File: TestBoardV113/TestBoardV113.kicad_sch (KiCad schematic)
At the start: 75 parts, among them J1 Conn_01x02_Socket, J10 Conn_01x02_Pin, J11 Conn_01x02_Pin, J12 Conn_02x03_Odd_Even, J13 Conn_01x01_Pin, J14 Conn_01x28_Socket, J15 Conn_01x01_Pin, J16 Conn_01x01_Pin, J17 Conn_01x02_Pin, J18 Conn_01x02_Socket, J19 Conn_01x28_Socket, J2 Conn_02x06_Odd_Even, J20 Conn_01x01_Pin, J21 Conn_01x02_Pin, J22 Conn_02x03_Odd_Even, J23 Conn_01x02_Pin, J24 Conn_01x02_Socket, J3 Conn_01x02_Pin, J4 Conn_01x02_Pin, J5 Conn_01x02_Pin, J6 Conn_01x02_Pin, J7 Conn_01x02_Pin, J8 Conn_01x02_Pin, J9 Conn_01x02_Pin, SW1 SW_DIP_x04, U3 NCP705MTADJTCG, U4 TAR5SxxU_SOT353F, U5 TXB0104PW, U6 TXB0104PW

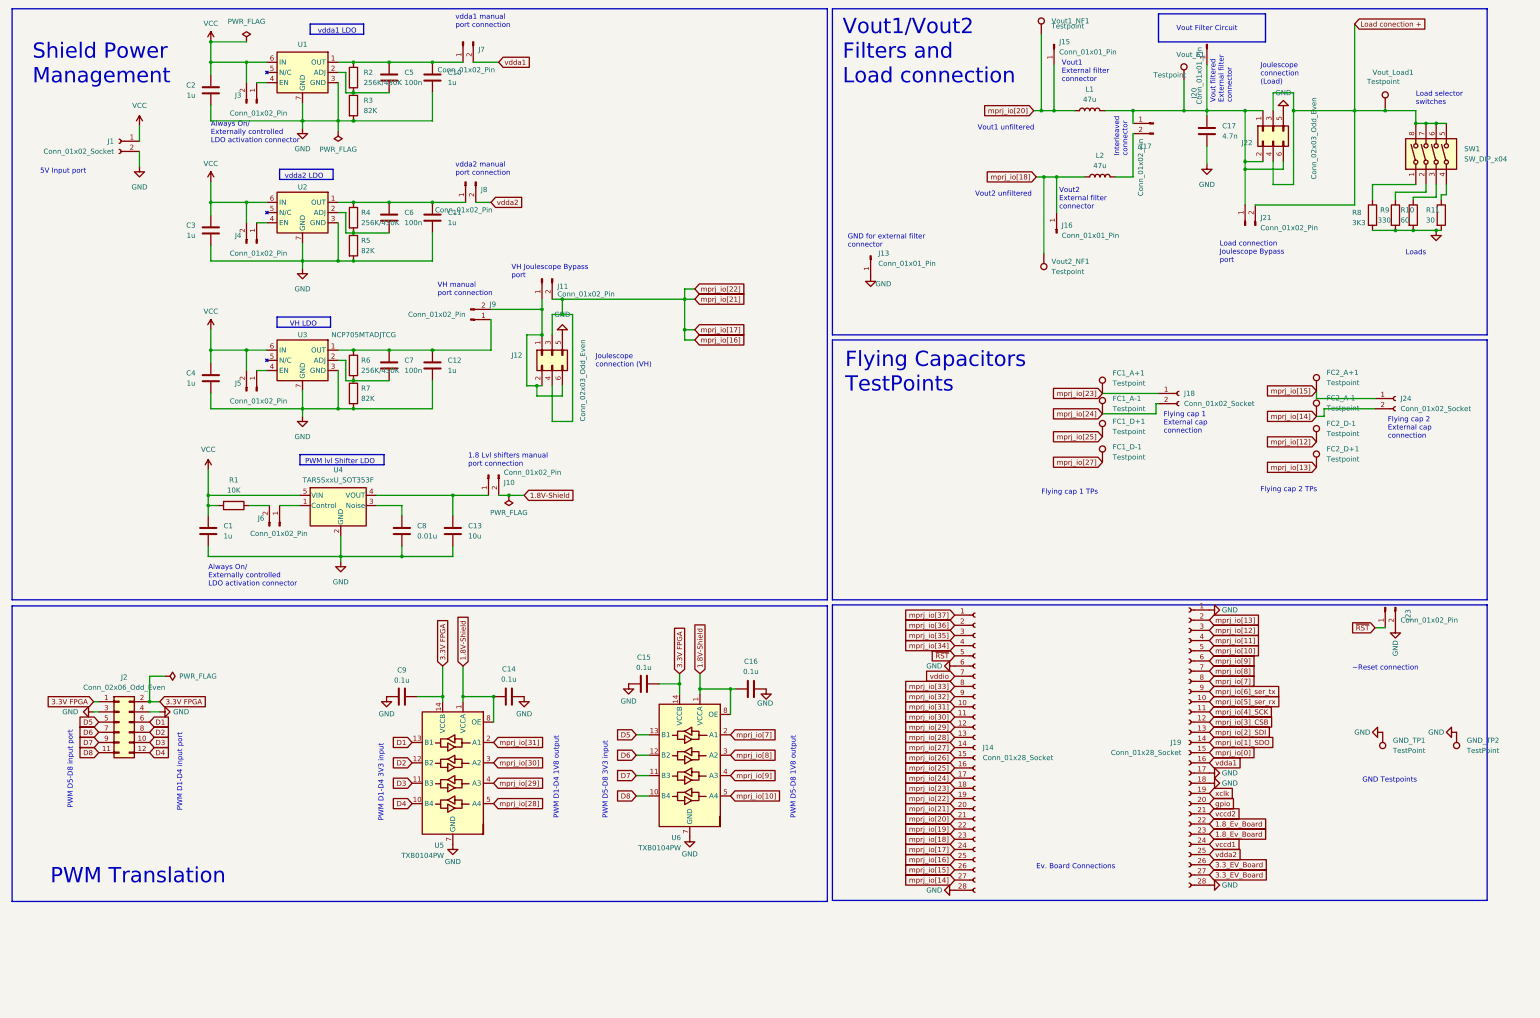
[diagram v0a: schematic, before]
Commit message: Added features
Added Joulescope port for efficiency measurement with and without level shifters
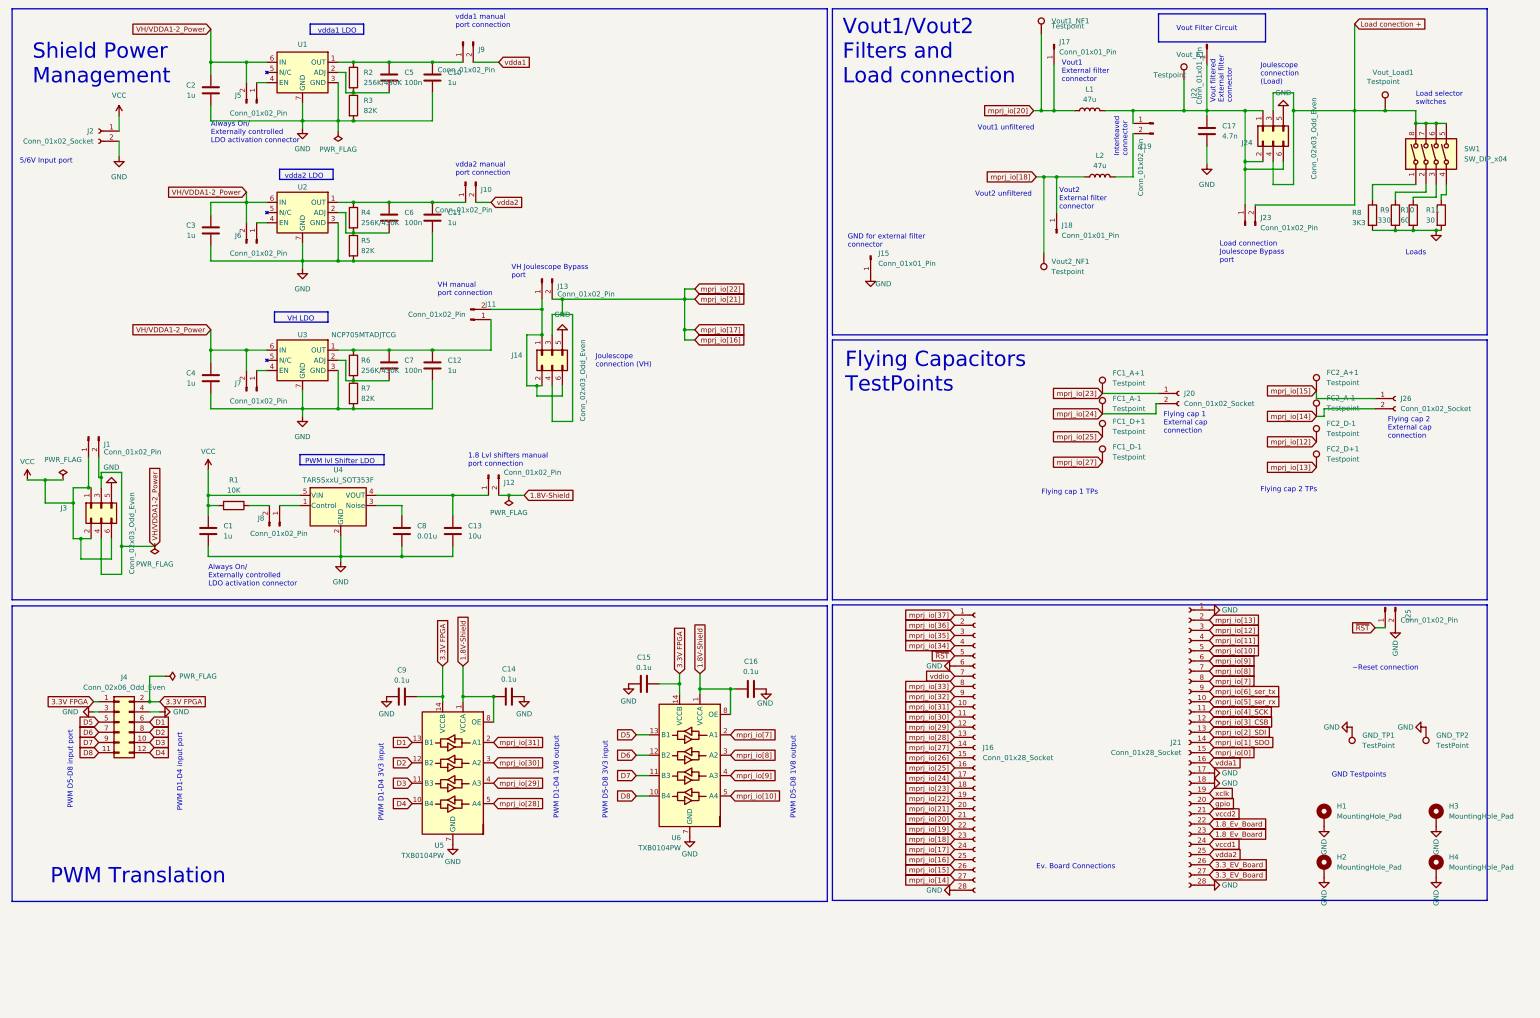
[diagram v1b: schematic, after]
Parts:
- added H1, H2, H3, H4: MountingHole_Pad, MountingHole:MountingHole_3.2mm_M3_DIN965_Pad, symbol Mechanical:MountingHole_Pad
- added J1: Conn_01x02_Pin, Connector_PinHeader_2.54mm:PinHeader_1x02_P2.54mm_Vertical, symbol Connector:Conn_01x02_Pin
- added J3: Conn_02x03_Odd_Even, Connector_PinHeader_2.54mm:PinHeader_2x03_P2.54mm_Vertical, symbol Connector_Generic:Conn_02x03_Odd_Even
- renumbered J8 to J10, J9 to J11, J10 to J12, J11 to J13, J12 to J14, J13 to J15, J14 to J16, J15 to J17, J16 to J18, J17 to J19, J1 to J2, J18 to J20, J19 to J21, J20 to J22, J21 to J23, J22 to J24, J23 to J25, J24 to J26, J2 to J4, J3 to J5, J4 to J6, J5 to J7, J6 to J8, J7 to J9
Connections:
- net GND: now also H1.1, H2.1, H3.1, H4.1, J3.5 (Pin_5)
- net VCC: now also J1.1 (Pin_1), J3.1 (Pin_1), J3.2 (Pin_2), J3.6 (Pin_6); no longer C2.1, C3.1, C4.1, J5.2 (Pin_2), J6.2 (Pin_2), J7.2 (Pin_2), U1.6 (IN), U2.6 (IN), U3.6 (IN)
- new net VH/VDDA1-2_Power: C2.1, C3.1, C4.1, J1.2 (Pin_2), J3.3 (Pin_3), J3.4 (Pin_4), J5.2 (Pin_2), J6.2 (Pin_2), J7.2 (Pin_2), U1.6 (IN), U2.6 (IN), U3.6 (IN)
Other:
- note added: "5/6V Input port"
- note removed: "5V Input port"
- moved on the sheet: GND_TP1, GND_TP2, J2

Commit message: Changed Items
Changed dip switch from 4
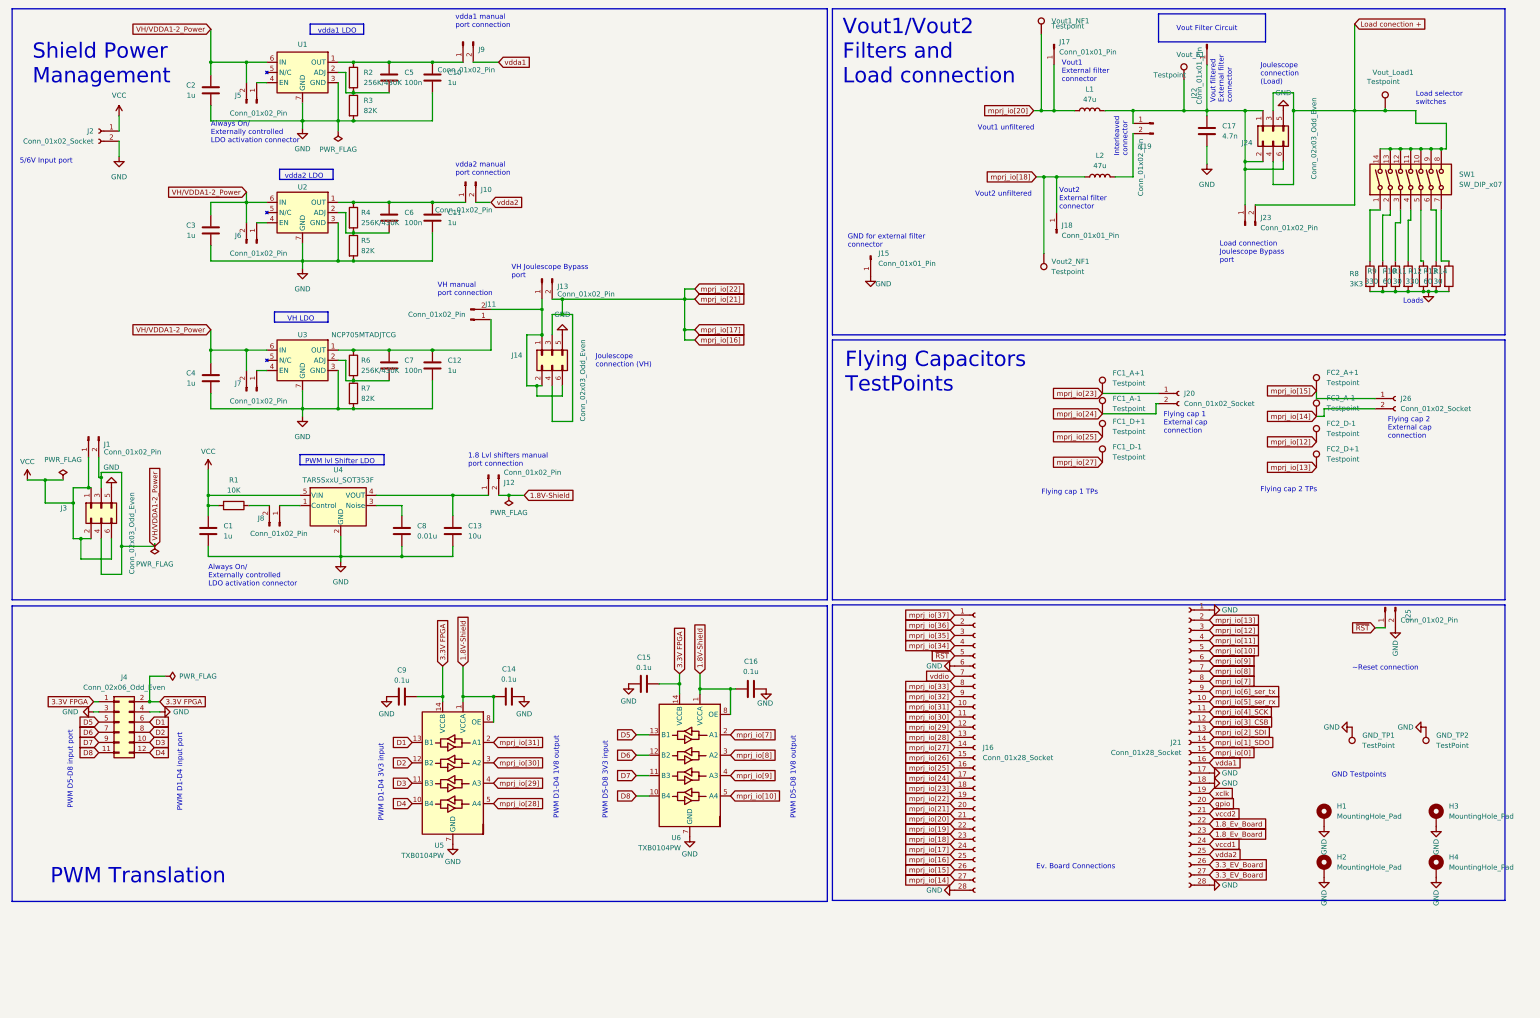
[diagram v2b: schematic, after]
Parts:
- removed SW1: SW_DIP_x04, Button_Switch_THT:SW_DIP_SPSTx04_Slide_9.78x12.34mm_W7.62mm_P2.54mm, symbol Switch:SW_DIP_x04
- added R12: 330, Resistor_SMD:R_1206_3216Metric, symbol Device:R
- added R13: 60, Resistor_SMD:R_1206_3216Metric, symbol Device:R
- added R14: 30, Resistor_SMD:R_1206_3216Metric, symbol Device:R
- added SW1: SW_DIP_x07, Button_Switch_THT:SW_DIP_SPSTx07_Slide_9.78x19.96mm_W7.62mm_P2.54mm, symbol Switch:SW_DIP_x07
- R10, R11, R8, R9: footprint Resistor_SMD:R_0805_2012Metric -> Resistor_SMD:R_1206_3216Metric
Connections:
- net GND: now also R12.2, R13.2, R14.2
- net Load conection +: now also SW1.10, SW1.11, SW1.12, SW1.13, SW1.14, SW1.8, SW1.9
- net at R8.1: now also SW1.1
- net at R9.1: now also SW1.2
- net at R10.1: now also SW1.3
- net at R11.1: now also SW1.4
- new net: R13.1, SW1.6
- new net: R12.1, SW1.5
- new net: R14.1, SW1.7

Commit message: Changed Items
Added independent joulescope connection for vdda1 and 2, added testpoints for 1.8V pwm signals
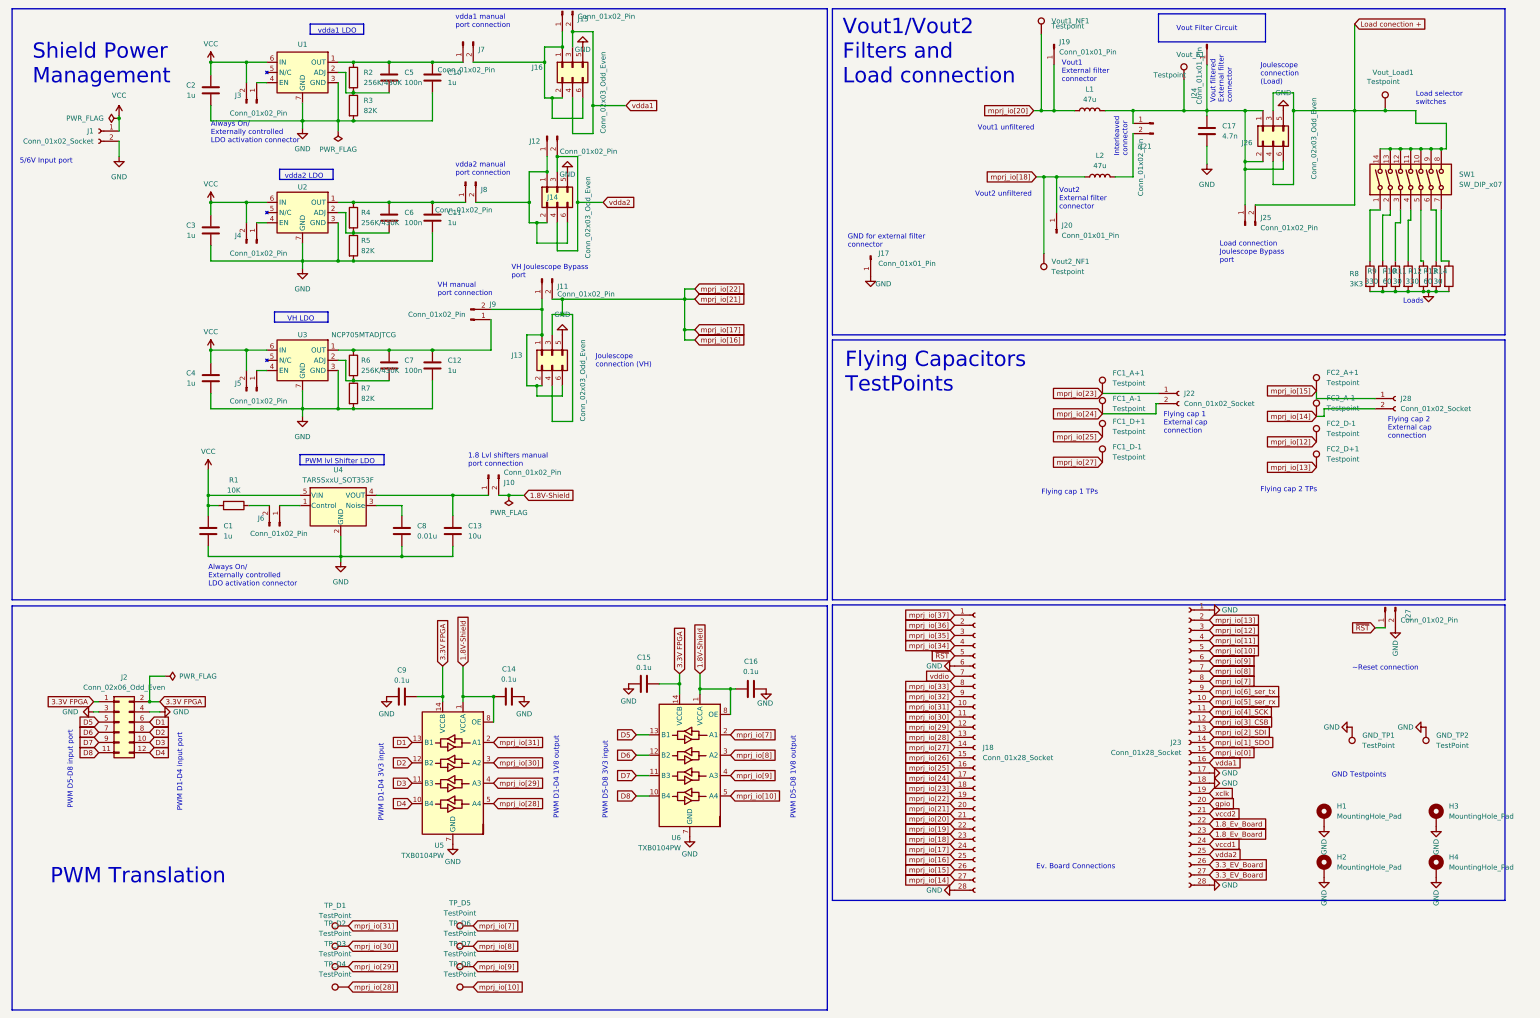
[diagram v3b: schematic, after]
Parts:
- added J12: Conn_01x02_Pin, Connector_PinHeader_2.54mm:PinHeader_1x02_P2.54mm_Vertical, symbol Connector:Conn_01x02_Pin
- added J14: Conn_02x03_Odd_Even, Connector_PinHeader_2.54mm:PinHeader_2x03_P2.54mm_Vertical, symbol Connector_Generic:Conn_02x03_Odd_Even
- added TP_D1, TP_D2, TP_D3, TP_D4, TP_D5, TP_D6, TP_D7, TP_D8: TestPoint, TestPoint:TestPoint_Keystone_5019_Minature, symbol Connector:TestPoint
- renumbered J2 to J1, J12 to J10, J13 to J11, J14 to J13, J1 to J15, J3 to J16, J15 to J17, J16 to J18, J17 to J19, J4 to J2, J18 to J20, J19 to J21, J20 to J22, J21 to J23, J22 to J24, J23 to J25, J24 to J26, J25 to J27, J26 to J28, J5 to J3, J6 to J4, J7 to J5, J8 to J6, J9 to J7, J10 to J8, J11 to J9
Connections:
- net GND: now also J14.5 (Pin_5)
- net VCC: now also C2.1, C3.1, C4.1, J3.2 (Pin_2), J4.2 (Pin_2), J5.2 (Pin_2), U1.6 (IN), U2.6 (IN), U3.6 (IN); no longer J15.1 (Pin_1), J16.1 (Pin_1), J16.2 (Pin_2), J16.6 (Pin_6)
- net mprj_io[10]: now also TP_D8.1
- net mprj_io[28]: now also TP_D4.1
- net mprj_io[29]: now also TP_D3.1
- net mprj_io[30]: now also TP_D2.1
- net mprj_io[31]: now also TP_D1.1
- net mprj_io[7]: now also TP_D5.1
- net mprj_io[8]: now also TP_D6.1
- net mprj_io[9]: now also TP_D7.1
- net vdda1: now also J15.2 (Pin_2), J16.3 (Pin_3), J16.4 (Pin_4); no longer J7.2 (Pin_2)
- net vdda2: now also J12.2 (Pin_2), J14.3 (Pin_3), J14.4 (Pin_4); no longer J8.2 (Pin_2)
- removed net VH/VDDA1-2_Power: C2.1, C3.1, C4.1, J15.2 (Pin_2), J16.3 (Pin_3), J16.4 (Pin_4), J3.2 (Pin_2), J4.2 (Pin_2), J5.2 (Pin_2), U1.6 (IN), U2.6 (IN), U3.6 (IN)
- new net: J12.1 (Pin_1), J14.1 (Pin_1), J14.2 (Pin_2), J14.6 (Pin_6), J8.2 (Pin_2)
- new net: J15.1 (Pin_1), J16.1 (Pin_1), J16.2 (Pin_2), J16.6 (Pin_6), J7.2 (Pin_2)
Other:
- moved on the sheet: J15, J16
